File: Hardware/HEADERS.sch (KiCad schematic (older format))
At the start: 16 parts, among them J1 CONN_01X03, J2 CONN_01X04

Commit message: Fixed some BOM stuff
fixed BOM for non RLC components
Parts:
- removed SPOX-1: AIRSPD, symbol SPOX-3
- removed SPOX-10: USART2, symbol SPOX-5
- removed SPOX-11: USART3, symbol SPOX-5
- removed SPOX-12: SPI1, symbol SPOX-6
- removed SPOX-13: SPI4, symbol SPOX-6
- removed SPOX-14: SPI5, symbol SPOX-6
- removed SPOX-2: EXT_BATT, symbol SPOX-2
- removed SPOX-3: DBG_SAFETY, symbol SPOX-3
- removed SPOX-4: I2C1, symbol SPOX-4
- removed SPOX-5: I2C2, symbol SPOX-4
- removed SPOX-6: I2C4, symbol SPOX-4
- removed SPOX-7: UART1, symbol SPOX-6
- removed SPOX-8: UART4, symbol SPOX-6
- removed SPOX-9: UART7, symbol SPOX-6
- added J18, J21, J22: SPOX-3, symbol SPOX-3
- added J20: SPOX-2, symbol SPOX-2
- added J23, J24, J25, J26, J27: SPOX-4, symbol SPOX-4
- added J28, J29, J30, J31, J33, J34, J35, J36: SPOX-6, symbol SPOX-6
- added J32: CONN_01X02, symbol CONN_01X02
- added R48, R49, R50, R51, R52, R53: 10K, symbol R
- J17: renamed from J1; part_num (none) -> CONN-007
- J19: renamed from J2; part_num (none) -> CONN-008
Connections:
- net labels added: DBG_CK, DBG_RX_PILOT, DBG_TX_PILOT, NRST_PILOT, NRST_SAFETY, SCLK_PILOT, SCLK_SAFETY, SPI2_CK, SPI2_SDO, SPI2_SI, SPI2_SS, SWIO_PILOT, SWIO_SAFETY, UART2_CTS, UART2_RTS, UART2_RX, UART2_TX
- net labels removed: USART2_RX, USART2_TX, USART3_CK, USART3_RX, USART3_TX
- wire segments 84 -> 124
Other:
- note added: "USART CK pins"
- note removed: "TODO JTAG"
- note removed: "TODO Safety programmer"

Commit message: Finished RLC bom stuff
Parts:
- R48, R49, R50, R51, R52, R53: part_num (none) -> RESS-005
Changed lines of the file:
@@
 SCLK_SAFETY
-$Comp
-L R R51
-U 1 1 59526B03
-P 3200 3450
-F 0 "R51" V 3280 3450 50  0000 C CNN
-F 1 "10K" V 3200 3450 50  0000 C CNN
-F 2 "" V 3130 3450 50  0001 C CNN
-F 3 "" H 3200 3450 50  0001 C CNN
-	1    3200 3450
-	1    0    0    -1
-$EndComp
 $Comp
 L R R48
@@
 F 2 "" V 2930 3450 50  0001 C CNN
 F 3 "" H 3000 3450 50  0001 C CNN
+F 4 "RESS-005" V 3000 3450 60  0001 C CNN "part_num"
 	1    3000 3450
-	1    0    0    -1
-$EndComp
-$Comp
-L R R52
-U 1 1 59526B9D
-P 3200 4050
-F 0 "R52" V 3280 4050 50  0000 C CNN
-F 1 "10K" V 3200 4050 50  0000 C CNN
-F 2 "" V 3130 4050 50  0001 C CNN
-F 3 "" H 3200 4050 50  0001 C CNN
-	1    3200 4050
-	1    0    0    -1
-$EndComp
-$Comp
-L R R49
-U 1 1 59526BE0
-P 3000 4050
-F 0 "R49" V 3080 4050 50  0000 C CNN
-F 1 "10K" V 3000 4050 50  0000 C CNN
-F 2 "" V 2930 4050 50  0001 C CNN
-F 3 "" H 3000 4050 50  0001 C CNN
-	1    3000 4050
-	1    0    0    -1
-$EndComp
-$Comp
-L R R53
-U 1 1 59526C01
-P 3200 4600
-F 0 "R53" V 3280 4600 50  0000 C CNN
-F 1 "10K" V 3200 4600 50  0000 C CNN
-F 2 "" V 3130 4600 50  0001 C CNN
-F 3 "" H 3200 4600 50  0001 C CNN
-	1    3200 4600
-	1    0    0    -1
-$EndComp
-$Comp
-L R R50
-U 1 1 59526C2A
-P 3000 4600
-F 0 "R50" V 3080 4600 50  0000 C CNN
-F 1 "10K" V 3000 4600 50  0000 C CNN
-F 2 "" V 2930 4600 50  0001 C CNN
-F 3 "" H 3000 4600 50  0001 C CNN
-	1    3000 4600
 	1    0    0    -1
 $EndComp
@@
 	1    0    0    -1
 $EndComp
+$Comp
+L R R51
+U 1 1 59595543
+P 3200 3450
+F 0 "R51" V 3280 3450 50  0000 C CNN
+F 1 "10K" V 3200 3450 50  0000 C CNN
+F 2 "" V 3130 3450 50  0001 C CNN
+F 3 "" H 3200 3450 50  0001 C CNN
+F 4 "RESS-005" V 3200 3450 60  0001 C CNN "part_num"
+	1    3200 3450
+	1    0    0    -1
+$EndComp
+$Comp
+L R R49
+U 1 1 5959558B
+P 3000 4050
+F 0 "R49" V 3080 4050 50  0000 C CNN
+F 1 "10K" V 3000 4050 50  0000 C CNN
+F 2 "" V 2930 4050 50  0001 C CNN
+F 3 "" H 3000 4050 50  0001 C CNN
+F 4 "RESS-005" V 3000 4050 60  0001 C CNN "part_num"
+	1    3000 4050
+	1    0    0    -1
+$EndComp
+$Comp
+L R R52
+U 1 1 595955DD
+P 3200 4050
+F 0 "R52" V 3280 4050 50  0000 C CNN
+F 1 "10K" V 3200 4050 50  0000 C CNN
+F 2 "" V 3130 4050 50  0001 C CNN
+F 3 "" H 3200 4050 50  0001 C CNN
+F 4 "RESS-005" V 3200 4050 60  0001 C CNN "part_num"
+	1    3200 4050
+	1    0    0    -1
+$EndComp
+$Comp
+L R R50
+U 1 1 59595625
+P 3000 4600
+F 0 "R50" V 3080 4600 50  0000 C CNN
+F 1 "10K" V 3000 4600 50  0000 C CNN
+F 2 "" V 2930 4600 50  0001 C CNN
+F 3 "" H 3000 4600 50  0001 C CNN
+F 4 "RESS-005" V 3000 4600 60  0001 C CNN "part_num"
+	1    3000 4600
+	1    0    0    -1
+$EndComp
+$Comp
+L R R53
+U 1 1 59595679
+P 3200 4600
+F 0 "R53" V 3280 4600 50  0000 C CNN
+F 1 "10K" V 3200 4600 50  0000 C CNN
+F 2 "" V 3130 4600 50  0001 C CNN
+F 3 "" H 3200 4600 50  0001 C CNN
+F 4 "RESS-005" V 3200 4600 60  0001 C CNN "part_num"
+	1    3200 4600
+	1    0    0    -1
+$EndComp

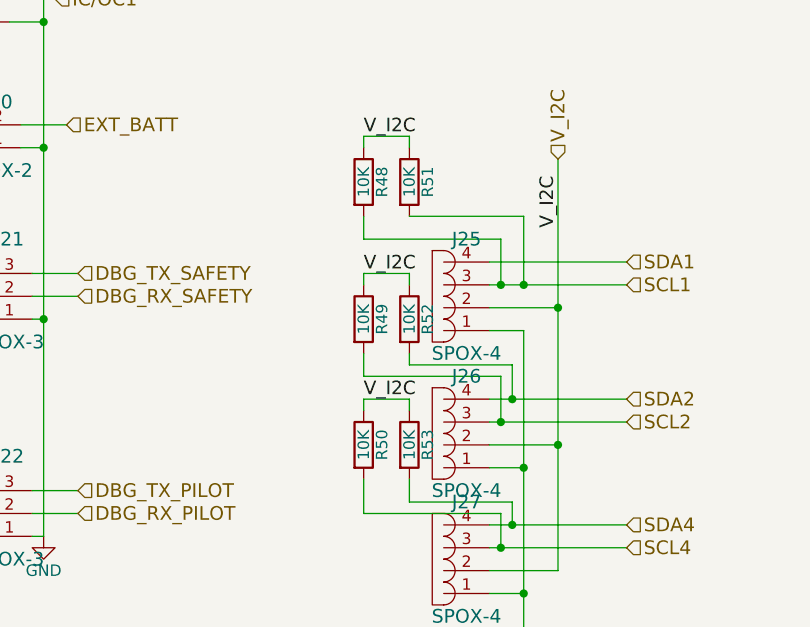
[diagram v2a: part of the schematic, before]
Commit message: Added ressistor footprint
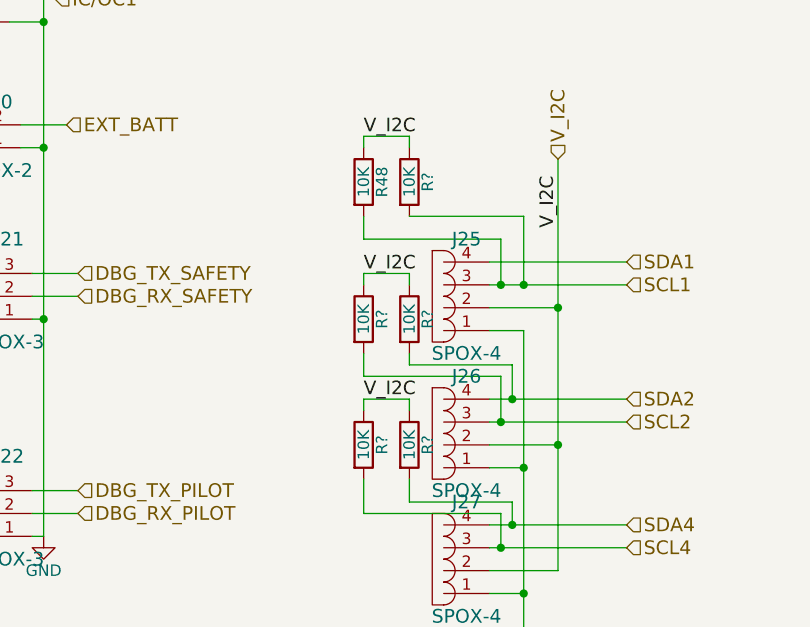
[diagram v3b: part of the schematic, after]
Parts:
- removed R49, R50, R51, R52, R53: 10K, symbol R
- added R? (x5): 10K, Resistors_SMD:R_0603_HandSoldering, symbol R
- R48: footprint (none) -> Resistors_SMD:R_0603_HandSoldering
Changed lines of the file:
@@
 F 0 "R48" V 3080 3450 50  0000 C CNN
 F 1 "10K" V 3000 3450 50  0000 C CNN
-F 2 "" V 2930 3450 50  0001 C CNN
+F 2 "Resistors_SMD:R_0603_HandSoldering" V 2930 3450 50  0001 C CNN
 F 3 "" H 3000 3450 50  0001 C CNN
 F 4 "RESS-005" V 3000 3450 60  0001 C CNN "part_num"
@@
 $EndComp
 $Comp
-L R R51
-U 1 1 59595543
+L R R?
+U 1 1 595B24C4
 P 3200 3450
-F 0 "R51" V 3280 3450 50  0000 C CNN
+F 0 "R?" V 3280 3450 50  0000 C CNN
 F 1 "10K" V 3200 3450 50  0000 C CNN
-F 2 "" V 3130 3450 50  0001 C CNN
+F 2 "Resistors_SMD:R_0603_HandSoldering" V 3130 3450 50  0001 C CNN
 F 3 "" H 3200 3450 50  0001 C CNN
 F 4 "RESS-005" V 3200 3450 60  0001 C CNN "part_num"
@@
 $EndComp
 $Comp
-L R R49
-U 1 1 5959558B
+L R R?
+U 1 1 595B2506
+P 3200 4050
+F 0 "R?" V 3280 4050 50  0000 C CNN
+F 1 "10K" V 3200 4050 50  0000 C CNN
+F 2 "Resistors_SMD:R_0603_HandSoldering" V 3130 4050 50  0001 C CNN
+F 3 "" H 3200 4050 50  0001 C CNN
+F 4 "RESS-005" V 3200 4050 60  0001 C CNN "part_num"
+	1    3200 4050
+	1    0    0    -1
+$EndComp
+$Comp
+L R R?
+U 1 1 595B2562
 P 3000 4050
-F 0 "R49" V 3080 4050 50  0000 C CNN
+F 0 "R?" V 3080 4050 50  0000 C CNN
 F 1 "10K" V 3000 4050 50  0000 C CNN
-F 2 "" V 2930 4050 50  0001 C CNN
+F 2 "Resistors_SMD:R_0603_HandSoldering" V 2930 4050 50  0001 C CNN
 F 3 "" H 3000 4050 50  0001 C CNN
 F 4 "RESS-005" V 3000 4050 60  0001 C CNN "part_num"
@@
 $EndComp
 $Comp
-L R R52
-U 1 1 595955DD
-P 3200 4050
-F 0 "R52" V 3280 4050 50  0000 C CNN
-F 1 "10K" V 3200 4050 50  0000 C CNN
-F 2 "" V 3130 4050 50  0001 C CNN
-F 3 "" H 3200 4050 50  0001 C CNN
-F 4 "RESS-005" V 3200 4050 60  0001 C CNN "part_num"
-	1    3200 4050
-	1    0    0    -1
-$EndComp
-$Comp
-L R R50
-U 1 1 59595625
+L R R?
+U 1 1 595B25FA
 P 3000 4600
-F 0 "R50" V 3080 4600 50  0000 C CNN
+F 0 "R?" V 3080 4600 50  0000 C CNN
 F 1 "10K" V 3000 4600 50  0000 C CNN
-F 2 "" V 2930 4600 50  0001 C CNN
+F 2 "Resistors_SMD:R_0603_HandSoldering" V 2930 4600 50  0001 C CNN
 F 3 "" H 3000 4600 50  0001 C CNN
 F 4 "RESS-005" V 3000 4600 60  0001 C CNN "part_num"
@@
 $EndComp
 $Comp
-L R R53
-U 1 1 59595679
+L R R?
+U 1 1 595B2654
 P 3200 4600
-F 0 "R53" V 3280 4600 50  0000 C CNN
+F 0 "R?" V 3280 4600 50  0000 C CNN
 F 1 "10K" V 3200 4600 50  0000 C CNN
-F 2 "" V 3130 4600 50  0001 C CNN
+F 2 "Resistors_SMD:R_0603_HandSoldering" V 3130 4600 50  0001 C CNN
 F 3 "" H 3200 4600 50  0001 C CNN
 F 4 "RESS-005" V 3200 4600 60  0001 C CNN "part_num"

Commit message: PCB?!
Added initial PCB file with ratsnest. footprint library still needs to
be setup.
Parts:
- J17: footprint (none) -> Pin_Headers:Pin_Header_Straight_1x03_Pitch2.54mm
- J18, J21, J22: footprint (none) -> Connectors_Molex:Molex_SPOX-5267_22-03-5035_03x2.54mm_Straight
- J19: footprint (none) -> Pin_Headers:Pin_Header_Straight_1x04_Pitch2.54mm
- J20: footprint (none) -> Connectors_Molex:Molex_SPOX-5267_22-03-5025_02x2.54mm_Straight
- J23, J24, J25, J26, J27: footprint (none) -> Connectors_Molex:Molex_SPOX-5267_22-03-5045_04x2.54mm_Straight
- J28, J29, J30, J31, J33, J34, J35, J36: footprint (none) -> Connectors_Molex:Molex_SPOX-5267_22-03-5065_06x2.54mm_Straight
- J32: footprint (none) -> Pin_Headers:Pin_Header_Straight_1x02_Pitch2.54mm
- gave numbers to parts that had none: 5
- renumbered R48 to R72

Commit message: Fixed serge suggestions
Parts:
- removed J17: CONN_01X03, Pin_Headers:Pin_Header_Straight_1x03_Pitch2.54mm, symbol CONN_01X03
- removed J19: CONN_01X04, Pin_Headers:Pin_Header_Straight_1x04_Pitch2.54mm, symbol CONN_01X04
- removed J23, J24: SPOX-4, Connectors_Molex:Molex_SPOX-5267_22-03-5045_04x2.54mm_Straight, symbol SPOX-4
- added J17: SPOX-3, Connectors_Molex:Molex_SPOX-5267_22-03-5035_03x2.54mm_Straight, symbol SPOX-3
- added J19: SPOX-4, Connectors_Molex:Molex_SPOX-5267_22-03-5045_04x2.54mm_Straight, symbol SPOX-4
- added J23, J24: SPOX-5, Connectors_Molex:Molex_SPOX-5267_22-03-5055_05x2.54mm_Straight, symbol SPOX-5
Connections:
- net labels added: V_PROG
- wire segments 124 -> 128
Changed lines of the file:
@@
 $Descr A4 11693 8268
 encoding utf-8
-Sheet 16 20
+Sheet 16 21
 Title ""
 Date ""
@@
 DBG_TX_SAFETY
 $Comp
-L GND #PWR43
+L GND #PWR041
 U 1 1 5923E07E
 P 3700 5400
-F 0 "#PWR43" H 3700 5150 50  0001 C CNN
+F 0 "#PWR041" H 3700 5150 50  0001 C CNN
 F 1 "GND" H 3700 5250 50  0000 C CNN
 F 2 "" H 3700 5400 50  0001 C CNN
@@
 SCL4
 $Comp
-L GND #PWR44
+L GND #PWR042
 U 1 1 5923E229
 P 6500 5700
-F 0 "#PWR44" H 6500 5450 50  0001 C CNN
+F 0 "#PWR042" H 6500 5450 50  0001 C CNN
 F 1 "GND" H 6500 5550 50  0000 C CNN
 F 2 "" H 6500 5700 50  0001 C CNN
@@
 SPI5_CK
 $Comp
-L GND #PWR45
+L GND #PWR043
 U 1 1 5923EE9C
 P 9950 5850
-F 0 "#PWR45" H 9950 5600 50  0001 C CNN
+F 0 "#PWR043" H 9950 5600 50  0001 C CNN
 F 1 "GND" H 9950 5700 50  0000 C CNN
 F 2 "" H 9950 5850 50  0001 C CNN
@@
 $EndComp
 $Comp
-L GND #PWR41
+L GND #PWR044
 U 1 1 5923F1BC
 P 1600 5000
-F 0 "#PWR41" H 1600 4750 50  0001 C CNN
+F 0 "#PWR044" H 1600 4750 50  0001 C CNN
 F 1 "GND" H 1600 4850 50  0000 C CNN
 F 2 "" H 1600 5000 50  0001 C CNN
@@
 	1    1600 5000
 	1    0    0    -1
-$EndComp
-$Comp
-L CONN_01X04 J19
-U 1 1 5923F1C9
-P 1250 2600
-F 0 "J19" H 1250 2850 50  0000 C CNN
-F 1 "CONN_01X04" V 1350 2600 50  0000 C CNN
-F 2 "Pin_Headers:Pin_Header_Straight_1x04_Pitch2.54mm" H 1250 2600 50  0001 C CNN
-F 3 "" H 1250 2600 50  0001 C CNN
-F 4 "CONN-008" H 1250 2600 60  0001 C CNN "part_num"
-	1    1250 2600
-	-1   0    0    1
 $EndComp
 Text HLabel 1650 2650 2    60   Input ~ 0
@@
 Text HLabel 1700 2000 2    60   Input ~ 0
 AIRSPD
-$Comp
-L CONN_01X03 J17
-U 1 1 5927D7FA
-P 1200 1400
-F 0 "J17" H 1200 1600 50  0000 C CNN
-F 1 "CONN_01X03" V 1300 1400 50  0000 C CNN
-F 2 "Pin_Headers:Pin_Header_Straight_1x03_Pitch2.54mm" H 1200 1400 50  0001 C CNN
-F 3 "" H 1200 1400 50  0001 C CNN
-F 4 "CONN-007" H 1200 1400 60  0001 C CNN "part_num"
-	1    1200 1400
-	-1   0    0    1
-$EndComp
 Text HLabel 1650 1400 2    60   Input ~ 0
 V_PPM
@@
 DBG_TX_PILOT
 $Comp
-L GND #PWR42
+L GND #PWR045
 U 1 1 594AA8BD
 P 1700 6950
-F 0 "#PWR42" H 1700 6700 50  0001 C CNN
+F 0 "#PWR045" H 1700 6700 50  0001 C CNN
 F 1 "GND" H 1700 6800 50  0000 C CNN
 F 2 "" H 1700 6950 50  0001 C CNN
@@
 $EndComp
 $Comp
-L SPOX-4 J23
-U 1 1 595BDAC3
-P 1350 5750
-F 0 "J23" H 1450 6000 60  0000 C CNN
-F 1 "SPOX-4" H 1450 5500 60  0000 C CNN
-F 2 "Connectors_Molex:Molex_SPOX-5267_22-03-5045_04x2.54mm_Straight" H 1350 5800 60  0001 C CNN
-F 3 "" H 1350 5800 60  0001 C CNN
-F 4 "CONN-003" H 1550 6100 60  0001 C CNN "part_num"
-	1    1350 5750
-	1    0    0    -1
-$EndComp
-$Comp
-L SPOX-4 J24
-U 1 1 595BDB1A
-P 1350 6500
-F 0 "J24" H 1450 6750 60  0000 C CNN
-F 1 "SPOX-4" H 1450 6250 60  0000 C CNN
-F 2 "Connectors_Molex:Molex_SPOX-5267_22-03-5045_04x2.54mm_Straight" H 1350 6550 60  0001 C CNN
-F 3 "" H 1350 6550 60  0001 C CNN
-F 4 "CONN-003" H 1550 6850 60  0001 C CNN "part_num"
-	1    1350 6500
-	1    0    0    -1
-$EndComp
-$Comp
 L SPOX-6 J28
 U 1 1 595BDC13
@@
 	1    0    0    -1
 $EndComp
+$Comp
+L SPOX-3 J17
+U 1 1 5966BE07
+P 1200 1400
+F 0 "J17" H 1300 1650 60  0000 C CNN
+F 1 "SPOX-3" H 1300 1200 60  0000 C CNN
+F 2 "Connectors_Molex:Molex_SPOX-5267_22-03-5035_03x2.54mm_Straight" H 1200 1550 60  0001 C CNN
+F 3 "" H 1300 1650 60  0001 C CNN
+F 4 "CONN-002" H 1400 1750 60  0001 C CNN "part_num"
+	1    1200 1400
+	1    0    0    -1
+$EndComp
+$Comp
+L SPOX-4 J19
+U 1 1 5966BE8B
+P 1250 2600
+F 0 "J19" H 1350 2850 60  0000 C CNN
+F 1 "SPOX-4" H 1350 2350 60  0000 C CNN
+F 2 "Connectors_Molex:Molex_SPOX-5267_22-03-5045_04x2.54mm_Straight" H 1250 2650 60  0001 C CNN
+F 3 "" H 1250 2650 60  0001 C CNN
+F 4 "CONN-003" H 1450 2950 60  0001 C CNN "part_num"
+	1    1250 2600
+	1    0    0    -1
+$EndComp
+$Comp
+L SPOX-5 J24
+U 1 1 59679B5A
+P 1350 6450
+F 0 "J24" H 1450 6750 60  0000 C CNN
+F 1 "SPOX-5" H 1450 6150 60  0000 C CNN
+F 2 "Connectors_Molex:Molex_SPOX-5267_22-03-5055_05x2.54mm_Straight" H 1350 6550 60  0001 C CNN
+F 3 "" H 1350 6550 60  0001 C CNN
+F 4 "CONN-004" H 1550 6850 60  0001 C CNN "part_num"
+	1    1350 6450
+	1    0    0    -1
+$EndComp
+$Comp
+L SPOX-5 J23
+U 1 1 59679BBF
+P 1350 5700
+F 0 "J23" H 1450 6000 60  0000 C CNN
+F 1 "SPOX-5" H 1450 5400 60  0000 C CNN
+F 2 "Connectors_Molex:Molex_SPOX-5267_22-03-5055_05x2.54mm_Straight" H 1350 5800 60  0001 C CNN
+F 3 "" H 1350 5800 60  0001 C CNN
+F 4 "CONN-004" H 1550 6100 60  0001 C CNN "part_num"
+	1    1350 5700
+	1    0    0    -1
+$EndComp
+Wire Wire Line
+	1550 5500 1800 5500
+Wire Wire Line
+	1800 5350 1800 6250
+Wire Wire Line
+	1800 6250 1550 6250
+Text HLabel 1850 5350 2    60   Input ~ 0
+V_PROG
+Wire Wire Line
+	1850 5350 1800 5350
+Connection ~ 1800 5500
 $EndSCHEMATC

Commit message: commit before my computer restarts
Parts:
- added J21: SPOX-3, Connectors_Molex:Molex_SPOX-5267_22-03-5035_03x2.54mm_Straight, symbol SPOX-3
- renumbered J17 to J16, J18 to J17, J19 to J18, J20 to J19, J21 to J20, R72 to R30, R73 to R31, R74 to R32, R75 to R33, R76 to R34, R77 to R35
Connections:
- net labels added: UHF_RX, UHF_TX
- wire segments 128 -> 131
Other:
- moved on the sheet: J20
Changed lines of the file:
@@
 Text HLabel 1700 3200 2    60   Input ~ 0
 EXT_BATT
-Text HLabel 1750 3950 2    60   Input ~ 0
+Text HLabel 1750 3800 2    60   Input ~ 0
 DBG_RX_SAFETY
-Text HLabel 1750 3850 2    60   Input ~ 0
+Text HLabel 1750 3700 2    60   Input ~ 0
 DBG_TX_SAFETY
 $Comp
@@
 $EndComp
 Text HLabel 1750 4900 2    60   Input ~ 0
-DBG_RX_PILOT
-Text HLabel 1750 4800 2    60   Input ~ 0
-DBG_TX_PILOT
+UHF_RX
 $Comp
 L GND #PWR045
@@
 SCLK_SAFETY
 $Comp
-L R R72
+L R R30
 U 1 1 59526B7D
 P 3000 3450
-F 0 "R72" V 3080 3450 50  0000 C CNN
+F 0 "R30" V 3080 3450 50  0000 C CNN
 F 1 "10K" V 3000 3450 50  0000 C CNN
 F 2 "Resistors_SMD:R_0603_HandSoldering" V 2930 3450 50  0001 C CNN
@@
 	1700 3200 1500 3200
 Wire Wire Line
-	1600 4050 1550 4050
-Wire Wire Line
-	1750 3850 1550 3850
-Wire Wire Line
-	1750 3950 1550 3950
+	1600 3900 1500 3900
+Wire Wire Line
+	1750 3700 1500 3700
+Wire Wire Line
+	1750 3800 1500 3800
 Wire Wire Line
 	3550 4100 3700 4100
@@
 Connection ~ 9950 5650
 Connection ~ 9950 4800
-Connection ~ 1600 4050
+Connection ~ 1600 3900
 Wire Wire Line
 	1600 2750 1450 2750
@@
 USART CK pins
 $Comp
-L R R75
+L R R33
 U 1 1 595B24C4
 P 3200 3450
-F 0 "R75" V 3280 3450 50  0000 C CNN
+F 0 "R33" V 3280 3450 50  0000 C CNN
 F 1 "10K" V 3200 3450 50  0000 C CNN
 F 2 "Resistors_SMD:R_0603_HandSoldering" V 3130 3450 50  0001 C CNN
@@
 $EndComp
 $Comp
-L R R76
+L R R34
 U 1 1 595B2506
 P 3200 4050
-F 0 "R76" V 3280 4050 50  0000 C CNN
+F 0 "R34" V 3280 4050 50  0000 C CNN
 F 1 "10K" V 3200 4050 50  0000 C CNN
 F 2 "Resistors_SMD:R_0603_HandSoldering" V 3130 4050 50  0001 C CNN
@@
 $EndComp
 $Comp
-L R R73
+L R R31
 U 1 1 595B2562
 P 3000 4050
-F 0 "R73" V 3080 4050 50  0000 C CNN
+F 0 "R31" V 3080 4050 50  0000 C CNN
 F 1 "10K" V 3000 4050 50  0000 C CNN
 F 2 "Resistors_SMD:R_0603_HandSoldering" V 2930 4050 50  0001 C CNN
@@
 $EndComp
 $Comp
-L R R74
+L R R32
 U 1 1 595B25FA
 P 3000 4600
-F 0 "R74" V 3080 4600 50  0000 C CNN
+F 0 "R32" V 3080 4600 50  0000 C CNN
 F 1 "10K" V 3000 4600 50  0000 C CNN
 F 2 "Resistors_SMD:R_0603_HandSoldering" V 2930 4600 50  0001 C CNN
@@
 $EndComp
 $Comp
-L R R77
+L R R35
 U 1 1 595B2654
 P 3200 4600
-F 0 "R77" V 3280 4600 50  0000 C CNN
+F 0 "R35" V 3280 4600 50  0000 C CNN
 F 1 "10K" V 3200 4600 50  0000 C CNN
 F 2 "Resistors_SMD:R_0603_HandSoldering" V 3130 4600 50  0001 C CNN
@@
 $EndComp
 $Comp
-L SPOX-2 J20
+L SPOX-2 J19
 U 1 1 595BD7F5
 P 1300 3250
-F 0 "J20" H 1400 3400 60  0000 C CNN
+F 0 "J19" H 1400 3400 60  0000 C CNN
 F 1 "SPOX-2" H 1400 3100 60  0000 C CNN
 F 2 "Connectors_Molex:Molex_SPOX-5267_22-03-5025_02x2.54mm_Straight" H 1300 3200 60  0001 C CNN
@@
 $EndComp
 $Comp
-L SPOX-3 J18
+L SPOX-3 J17
 U 1 1 595BD83D
 P 1250 2000
-F 0 "J18" H 1350 2250 60  0000 C CNN
+F 0 "J17" H 1350 2250 60  0000 C CNN
 F 1 "SPOX-3" H 1350 1800 60  0000 C CNN
 F 2 "Connectors_Molex:Molex_SPOX-5267_22-03-5035_03x2.54mm_Straight" H 1250 2150 60  0001 C CNN
@@
 $EndComp
 $Comp
-L SPOX-3 J21
+L SPOX-3 J20
 U 1 1 595BD88E
-P 1350 3950
-F 0 "J21" H 1450 4200 60  0000 C CNN
-F 1 "SPOX-3" H 1450 3750 60  0000 C CNN
-F 2 "Connectors_Molex:Molex_SPOX-5267_22-03-5035_03x2.54mm_Straight" H 1350 4100 60  0001 C CNN
-F 3 "" H 1450 4200 60  0001 C CNN
-F 4 "CONN-002" H 1550 4300 60  0001 C CNN "part_num"
-	1    1350 3950
+P 1300 3800
+F 0 "J20" H 1400 4050 60  0000 C CNN
+F 1 "SPOX-3" H 1400 3600 60  0000 C CNN
+F 2 "Connectors_Molex:Molex_SPOX-5267_22-03-5035_03x2.54mm_Straight" H 1300 3950 60  0001 C CNN
+F 3 "" H 1400 4050 60  0001 C CNN
+F 4 "CONN-002" H 1500 4150 60  0001 C CNN "part_num"
+	1    1300 3800
 	1    0    0    -1
 $EndComp
@@
 $EndComp
 $Comp
-L SPOX-3 J17
+L SPOX-3 J16
 U 1 1 5966BE07
 P 1200 1400
-F 0 "J17" H 1300 1650 60  0000 C CNN
+F 0 "J16" H 1300 1650 60  0000 C CNN
 F 1 "SPOX-3" H 1300 1200 60  0000 C CNN
 F 2 "Connectors_Molex:Molex_SPOX-5267_22-03-5035_03x2.54mm_Straight" H 1200 1550 60  0001 C CNN
@@
 $EndComp
 $Comp
-L SPOX-4 J19
+L SPOX-4 J18
 U 1 1 5966BE8B
 P 1250 2600
-F 0 "J19" H 1350 2850 60  0000 C CNN
+F 0 "J18" H 1350 2850 60  0000 C CNN
 F 1 "SPOX-4" H 1350 2350 60  0000 C CNN
 F 2 "Connectors_Molex:Molex_SPOX-5267_22-03-5045_04x2.54mm_Straight" H 1250 2650 60  0001 C CNN
@@
 	1850 5350 1800 5350
 Connection ~ 1800 5500
+$Comp
+L SPOX-3 J21
+U 1 1 596BAB07
+P 1300 4350
+F 0 "J21" H 1400 4600 60  0000 C CNN
+F 1 "SPOX-3" H 1400 4150 60  0000 C CNN
+F 2 "Connectors_Molex:Molex_SPOX-5267_22-03-5035_03x2.54mm_Straight" H 1300 4500 60  0001 C CNN
+F 3 "" H 1400 4600 60  0001 C CNN
+F 4 "CONN-002" H 1500 4700 60  0001 C CNN "part_num"
+	1    1300 4350
+	1    0    0    -1
+$EndComp
+Wire Wire Line
+	1500 4450 1600 4450
+Connection ~ 1600 4450
+Text HLabel 1700 4350 2    60   Input ~ 0
+DBG_RX_PILOT
+Text HLabel 1700 4250 2    60   Input ~ 0
+DBG_TX_PILOT
+Wire Wire Line
+	1700 4250 1500 4250
+Wire Wire Line
+	1700 4350 1500 4350
+Text HLabel 1750 4800 2    60   Input ~ 0
+UHF_TX
 $EndSCHEMATC

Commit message: finished signal routing
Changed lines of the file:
@@
 	3200 3600 3700 3600
-Wire Wire Line
-	3700 3600 3700 3900
-Connection ~ 3700 3900
 Wire Wire Line
 	3200 4200 3200 4250
@@
 Text HLabel 1750 4800 2    60   Input ~ 0
 UHF_TX
+Wire Wire Line
+	3700 3600 3700 3800
+Connection ~ 3700 3800
 $EndSCHEMATC
